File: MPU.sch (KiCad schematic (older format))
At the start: 31 parts, among them P1 BL_PAD, P10 CONN_01X01, P11 CONN_01X04, P2 SWD_DAT, P3 SWD_CLK, P4 SWD_3V3, P5 SWD_GND, P6 SWD_RST, P7 CONN_01X01, P8 CONN_01X01, P9 CONN_01X01, SW1 SW_PUSH, SW2 SW_PUSH, U4 SAMD21E17A, Y1 32.768kHz

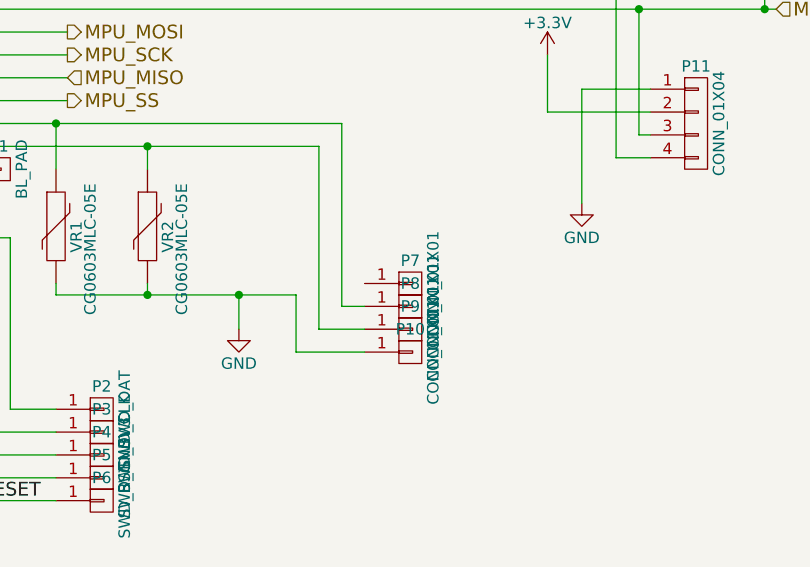
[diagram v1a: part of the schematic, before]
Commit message: moved battery input and fixed dodgy ground plane
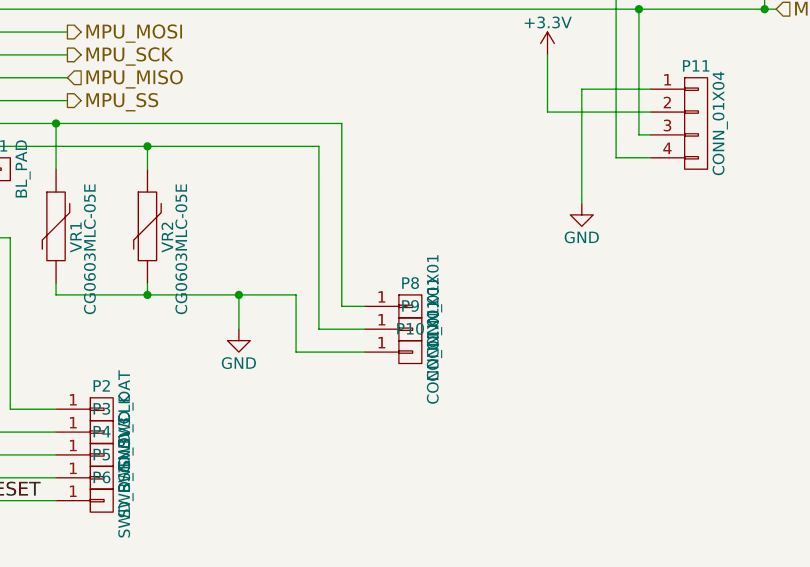
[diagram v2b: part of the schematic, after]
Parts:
- removed P7: CONN_01X01, Measurement_Points:Measurement_Point_Round-TH_Small, symbol CONN_01X01
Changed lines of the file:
@@
 $EndComp
 $Comp
-L GND #PWR013
+L GND #PWR26
 U 1 1 56C13132
 P 6950 4550
-F 0 "#PWR013" H 6950 4300 50  0001 C CNN
+F 0 "#PWR26" H 6950 4300 50  0001 C CNN
 F 1 "GND" H 6950 4400 50  0000 C CNN
 F 2 "" H 6950 4550 50  0000 C CNN
@@
 Connection ~ 2200 2050
 $Comp
-L GND #PWR014
+L GND #PWR15
 U 1 1 56C1336E
 P 1900 2650
-F 0 "#PWR014" H 1900 2400 50  0001 C CNN
+F 0 "#PWR15" H 1900 2400 50  0001 C CNN
 F 1 "GND" H 1900 2500 50  0000 C CNN
 F 2 "" H 1900 2650 50  0000 C CNN
@@
 $EndComp
 $Comp
-L GND #PWR015
+L GND #PWR16
 U 1 1 56C133A0
 P 2200 2650
-F 0 "#PWR015" H 2200 2400 50  0001 C CNN
+F 0 "#PWR16" H 2200 2400 50  0001 C CNN
 F 1 "GND" H 2200 2500 50  0000 C CNN
 F 2 "" H 2200 2650 50  0000 C CNN
@@
 $EndComp
 $Comp
-L GND #PWR016
+L GND #PWR18
 U 1 1 56C133D2
 P 2500 2650
-F 0 "#PWR016" H 2500 2400 50  0001 C CNN
+F 0 "#PWR18" H 2500 2400 50  0001 C CNN
 F 1 "GND" H 2500 2500 50  0000 C CNN
 F 2 "" H 2500 2650 50  0000 C CNN
@@
 $EndComp
 $Comp
-L +3V3 #PWR017
+L +3V3 #PWR30
 U 1 1 56C24D00
 P 9150 2500
-F 0 "#PWR017" H 9150 2350 50  0001 C CNN
+F 0 "#PWR30" H 9150 2350 50  0001 C CNN
 F 1 "+3V3" H 9150 2640 50  0000 C CNN
 F 2 "" H 9150 2500 50  0000 C CNN
@@
 $EndComp
 $Comp
-L GND #PWR018
+L GND #PWR25
 U 1 1 56C269FF
 P 6100 1400
-F 0 "#PWR018" H 6100 1150 50  0001 C CNN
+F 0 "#PWR25" H 6100 1150 50  0001 C CNN
 F 1 "GND" H 6100 1250 50  0000 C CNN
 F 2 "" H 6100 1400 50  0000 C CNN
@@
 AIN_6
 $Comp
-L GND #PWR019
+L GND #PWR21
 U 1 1 56C278AB
 P 4000 6000
-F 0 "#PWR019" H 4000 5750 50  0001 C CNN
+F 0 "#PWR21" H 4000 5750 50  0001 C CNN
 F 1 "GND" H 4000 5850 50  0000 C CNN
 F 2 "" H 4000 6000 50  0000 C CNN
@@
 	1550 3000 1550 3200
 $Comp
-L GND #PWR020
+L GND #PWR14
 U 1 1 56C282F2
 P 1550 3600
-F 0 "#PWR020" H 1550 3350 50  0001 C CNN
+F 0 "#PWR14" H 1550 3350 50  0001 C CNN
 F 1 "GND" H 1550 3450 50  0000 C CNN
 F 2 "" H 1550 3600 50  0000 C CNN
@@
 	1550 3500 1550 3600
 $Comp
-L +3V3 #PWR021
+L +3V3 #PWR13
 U 1 1 56C28419
 P 1550 3000
-F 0 "#PWR021" H 1550 2850 50  0001 C CNN
+F 0 "#PWR13" H 1550 2850 50  0001 C CNN
 F 1 "+3V3" H 1550 3140 50  0000 C CNN
 F 2 "" H 1550 3000 50  0000 C CNN
@@
 	2600 1650 2600 1550
 $Comp
-L +3V3 #PWR022
+L +3V3 #PWR19
 U 1 1 56C28F33
 P 2600 1150
-F 0 "#PWR022" H 2600 1000 50  0001 C CNN
+F 0 "#PWR19" H 2600 1000 50  0001 C CNN
 F 1 "+3V3" H 2600 1290 50  0000 C CNN
 F 2 "" H 2600 1150 50  0000 C CNN
@@
 	2600 1150 2600 1250
 $Comp
-L +3V3 #PWR023
+L +3V3 #PWR23
 U 1 1 56C2B080
 P 5350 5050
-F 0 "#PWR023" H 5350 4900 50  0001 C CNN
+F 0 "#PWR23" H 5350 4900 50  0001 C CNN
 F 1 "+3V3" H 5350 5190 50  0000 C CNN
 F 2 "" H 5350 5050 50  0000 C CNN
@@
 $EndComp
 $Comp
-L GND #PWR024
+L GND #PWR24
 U 1 1 56C2B0D0
 P 5350 5250
-F 0 "#PWR024" H 5350 5000 50  0001 C CNN
+F 0 "#PWR24" H 5350 5000 50  0001 C CNN
 F 1 "GND" H 5350 5100 50  0000 C CNN
 F 2 "" H 5350 5250 50  0000 C CNN
@@
 	5350 5200 6150 5200
 $Comp
-L +3V3 #PWR025
+L +3V3 #PWR17
 U 1 1 56C2B3B6
 P 2350 1900
-F 0 "#PWR025" H 2350 1750 50  0001 C CNN
+F 0 "#PWR17" H 2350 1750 50  0001 C CNN
 F 1 "+3V3" H 2350 2040 50  0000 C CNN
 F 2 "" H 2350 1900 50  0000 C CNN
@@
 Connection ~ 2350 2050
 $Comp
-L GND #PWR026
+L GND #PWR20
 U 1 1 56C39EB2
 P 2900 4300
-F 0 "#PWR026" H 2900 4050 50  0001 C CNN
+F 0 "#PWR20" H 2900 4050 50  0001 C CNN
 F 1 "GND" H 2900 4150 50  0000 C CNN
 F 2 "" H 2900 4300 50  0000 C CNN
@@
 	4700 6200 4700 6050
 $Comp
-L +3V3 #PWR027
+L +3V3 #PWR22
 U 1 1 56C3A13C
 P 4700 5100
-F 0 "#PWR027" H 4700 4950 50  0001 C CNN
+F 0 "#PWR22" H 4700 4950 50  0001 C CNN
 F 1 "+3V3" H 4700 5240 50  0000 C CNN
 F 2 "" H 4700 5100 50  0000 C CNN
@@
 F 3 "" H 6350 5300 50  0000 C CNN
 	1    6350 5300
-	1    0    0    -1
-$EndComp
-$Comp
-L CONN_01X01 P7
-U 1 1 56C3BDC8
-P 7700 4350
-F 0 "P7" H 7700 4450 50  0000 C CNN
-F 1 "CONN_01X01" V 7800 4350 50  0000 C CNN
-F 2 "Measurement_Points:Measurement_Point_Round-TH_Small" H 7700 4350 50  0001 C CNN
-F 3 "" H 7700 4350 50  0000 C CNN
-	1    7700 4350
 	1    0    0    -1
 $EndComp
@@
 $EndComp
 $Comp
-L GND #PWR028
+L GND #PWR28
 U 1 1 56EAE5DD
 P 8450 4000
-F 0 "#PWR028" H 8450 3750 50  0001 C CNN
+F 0 "#PWR28" H 8450 3750 50  0001 C CNN
 F 1 "GND" H 8450 3850 50  0000 C CNN
 F 2 "" H 8450 4000 50  0000 C CNN
@@
 $EndComp
 $Comp
-L +3.3V #PWR029
+L +3.3V #PWR27
 U 1 1 56EAE62B
 P 8300 3350
-F 0 "#PWR029" H 8300 3200 50  0001 C CNN
+F 0 "#PWR27" H 8300 3200 50  0001 C CNN
 F 1 "+3.3V" H 8300 3490 50  0000 C CNN
 F 2 "" H 8300 3350 50  0000 C CNN
@@
 $EndComp
 $Comp
-L GND #PWR030
+L GND #PWR29
 U 1 1 56EC2766
 P 8750 2600
-F 0 "#PWR030" H 8750 2350 50  0001 C CNN
+F 0 "#PWR29" H 8750 2350 50  0001 C CNN
 F 1 "GND" H 8750 2450 50  0000 C CNN
 F 2 "" H 8750 2600 50  0000 C CNN

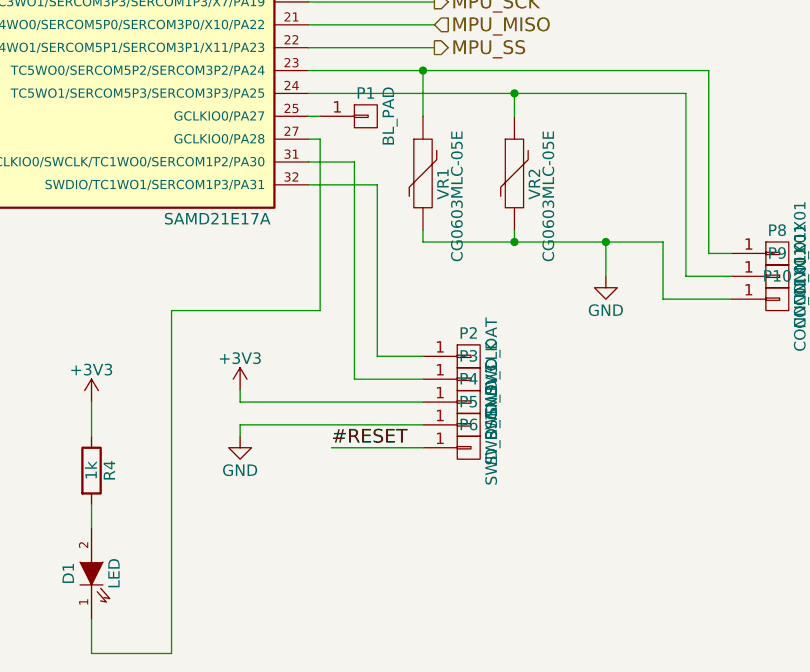
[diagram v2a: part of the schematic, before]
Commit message: Changed L3 to 0603, L2 to 3x3, Fixed P8 silk and made gerbers
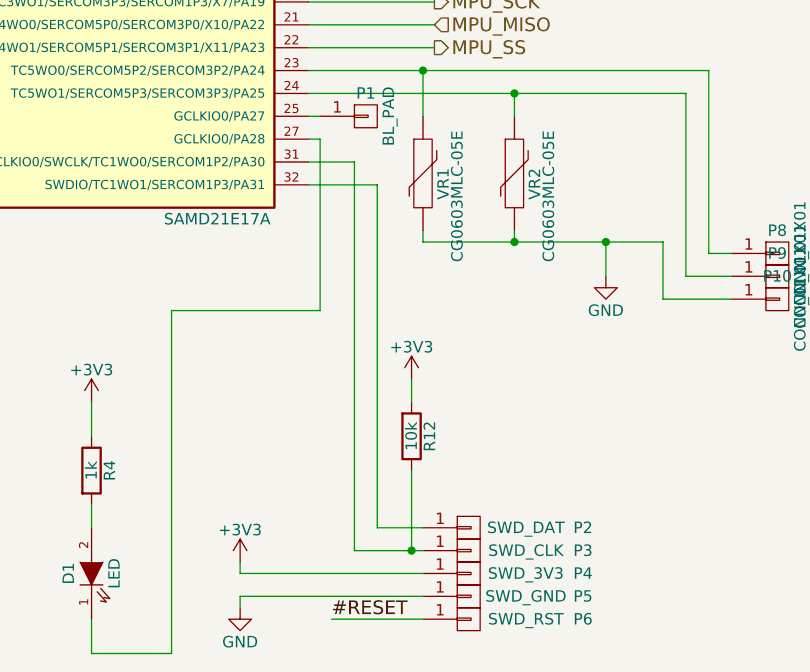
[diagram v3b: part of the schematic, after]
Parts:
- added R12: 10k, Capacitors_SMD:C_0603, symbol R
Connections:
- net +3V3: now also R12.2
- net at P3.1 (P1), U4.31 (GCLKIO0/SWCLK/TC1WO0/SERCOM1P2/PA30): now also R12.1
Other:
- moved on the sheet: P2, P3, P4, P5, P6
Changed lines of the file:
@@
 $EndComp
 $Comp
-L GND #PWR26
+L GND #PWR013
 U 1 1 56C13132
 P 6950 4550
-F 0 "#PWR26" H 6950 4300 50  0001 C CNN
+F 0 "#PWR013" H 6950 4300 50  0001 C CNN
 F 1 "GND" H 6950 4400 50  0000 C CNN
 F 2 "" H 6950 4550 50  0000 C CNN
@@
 Connection ~ 2200 2050
 $Comp
-L GND #PWR15
+L GND #PWR014
 U 1 1 56C1336E
 P 1900 2650
-F 0 "#PWR15" H 1900 2400 50  0001 C CNN
+F 0 "#PWR014" H 1900 2400 50  0001 C CNN
 F 1 "GND" H 1900 2500 50  0000 C CNN
 F 2 "" H 1900 2650 50  0000 C CNN
@@
 $EndComp
 $Comp
-L GND #PWR16
+L GND #PWR015
 U 1 1 56C133A0
 P 2200 2650
-F 0 "#PWR16" H 2200 2400 50  0001 C CNN
+F 0 "#PWR015" H 2200 2400 50  0001 C CNN
 F 1 "GND" H 2200 2500 50  0000 C CNN
 F 2 "" H 2200 2650 50  0000 C CNN
@@
 $EndComp
 $Comp
-L GND #PWR18
+L GND #PWR016
 U 1 1 56C133D2
 P 2500 2650
-F 0 "#PWR18" H 2500 2400 50  0001 C CNN
+F 0 "#PWR016" H 2500 2400 50  0001 C CNN
 F 1 "GND" H 2500 2500 50  0000 C CNN
 F 2 "" H 2500 2650 50  0000 C CNN
@@
 $EndComp
 $Comp
-L +3V3 #PWR30
+L +3V3 #PWR017
 U 1 1 56C24D00
 P 9150 2500
-F 0 "#PWR30" H 9150 2350 50  0001 C CNN
+F 0 "#PWR017" H 9150 2350 50  0001 C CNN
 F 1 "+3V3" H 9150 2640 50  0000 C CNN
 F 2 "" H 9150 2500 50  0000 C CNN
@@
 $EndComp
 $Comp
-L GND #PWR25
+L GND #PWR018
 U 1 1 56C269FF
 P 6100 1400
-F 0 "#PWR25" H 6100 1150 50  0001 C CNN
+F 0 "#PWR018" H 6100 1150 50  0001 C CNN
 F 1 "GND" H 6100 1250 50  0000 C CNN
 F 2 "" H 6100 1400 50  0000 C CNN
@@
 AIN_6
 $Comp
-L GND #PWR21
+L GND #PWR019
 U 1 1 56C278AB
 P 4000 6000
-F 0 "#PWR21" H 4000 5750 50  0001 C CNN
+F 0 "#PWR019" H 4000 5750 50  0001 C CNN
 F 1 "GND" H 4000 5850 50  0000 C CNN
 F 2 "" H 4000 6000 50  0000 C CNN
@@
 	1550 3000 1550 3200
 $Comp
-L GND #PWR14
+L GND #PWR020
 U 1 1 56C282F2
 P 1550 3600
-F 0 "#PWR14" H 1550 3350 50  0001 C CNN
+F 0 "#PWR020" H 1550 3350 50  0001 C CNN
 F 1 "GND" H 1550 3450 50  0000 C CNN
 F 2 "" H 1550 3600 50  0000 C CNN
@@
 	1550 3500 1550 3600
 $Comp
-L +3V3 #PWR13
+L +3V3 #PWR021
 U 1 1 56C28419
 P 1550 3000
-F 0 "#PWR13" H 1550 2850 50  0001 C CNN
+F 0 "#PWR021" H 1550 2850 50  0001 C CNN
 F 1 "+3V3" H 1550 3140 50  0000 C CNN
 F 2 "" H 1550 3000 50  0000 C CNN
@@
 	5650 4050 5850 4050
 Wire Wire Line
-	5850 4050 5850 5000
-Wire Wire Line
-	5850 5000 6150 5000
-Wire Wire Line
-	6150 4900 5950 4900
-Wire Wire Line
-	5950 4900 5950 4150
+	5850 4050 5850 5750
+Wire Wire Line
+	5850 5750 6150 5750
+Wire Wire Line
+	5950 5650 6150 5650
+Wire Wire Line
+	5950 4150 5950 5650
 Wire Wire Line
 	5950 4150 5650 4150
@@
 #RESET
 Wire Wire Line
-	6150 5300 5750 5300
-Text Label 5750 5300 0    60   ~ 0
+	6150 6050 5750 6050
+Text Label 5750 6050 0    60   ~ 0
 #RESET
 $Comp
@@
 	2600 1650 2600 1550
 $Comp
-L +3V3 #PWR19
+L +3V3 #PWR022
 U 1 1 56C28F33
 P 2600 1150
-F 0 "#PWR19" H 2600 1000 50  0001 C CNN
+F 0 "#PWR022" H 2600 1000 50  0001 C CNN
 F 1 "+3V3" H 2600 1290 50  0000 C CNN
 F 2 "" H 2600 1150 50  0000 C CNN
@@
 	2600 1150 2600 1250
 $Comp
-L +3V3 #PWR23
+L +3V3 #PWR023
 U 1 1 56C2B080
-P 5350 5050
-F 0 "#PWR23" H 5350 4900 50  0001 C CNN
-F 1 "+3V3" H 5350 5190 50  0000 C CNN
-F 2 "" H 5350 5050 50  0000 C CNN
-F 3 "" H 5350 5050 50  0000 C CNN
-	1    5350 5050
-	1    0    0    -1
-$EndComp
-$Comp
-L GND #PWR24
+P 5350 5800
+F 0 "#PWR023" H 5350 5650 50  0001 C CNN
+F 1 "+3V3" H 5350 5940 50  0000 C CNN
+F 2 "" H 5350 5800 50  0000 C CNN
+F 3 "" H 5350 5800 50  0000 C CNN
+	1    5350 5800
+	1    0    0    -1
+$EndComp
+$Comp
+L GND #PWR024
 U 1 1 56C2B0D0
-P 5350 5250
-F 0 "#PWR24" H 5350 5000 50  0001 C CNN
-F 1 "GND" H 5350 5100 50  0000 C CNN
-F 2 "" H 5350 5250 50  0000 C CNN
-F 3 "" H 5350 5250 50  0000 C CNN
-	1    5350 5250
-	1    0    0    -1
-$EndComp
-Wire Wire Line
-	5350 5050 5350 5100
-Wire Wire Line
-	5350 5100 6150 5100
-Wire Wire Line
-	5350 5250 5350 5200
-Wire Wire Line
-	5350 5200 6150 5200
-$Comp
-L +3V3 #PWR17
+P 5350 6000
+F 0 "#PWR024" H 5350 5750 50  0001 C CNN
+F 1 "GND" H 5350 5850 50  0000 C CNN
+F 2 "" H 5350 6000 50  0000 C CNN
+F 3 "" H 5350 6000 50  0000 C CNN
+	1    5350 6000
+	1    0    0    -1
+$EndComp
+Wire Wire Line
+	5350 5800 5350 5850
+Wire Wire Line
+	5350 5850 6150 5850
+Wire Wire Line
+	5350 6000 5350 5950
+Wire Wire Line
+	5350 5950 6150 5950
+$Comp
+L +3V3 #PWR025
 U 1 1 56C2B3B6
 P 2350 1900
-F 0 "#PWR17" H 2350 1750 50  0001 C CNN
+F 0 "#PWR025" H 2350 1750 50  0001 C CNN
 F 1 "+3V3" H 2350 2040 50  0000 C CNN
 F 2 "" H 2350 1900 50  0000 C CNN
@@
 Connection ~ 2350 2050
 $Comp
-L GND #PWR20
+L GND #PWR026
 U 1 1 56C39EB2
 P 2900 4300
-F 0 "#PWR20" H 2900 4050 50  0001 C CNN
+F 0 "#PWR026" H 2900 4050 50  0001 C CNN
 F 1 "GND" H 2900 4150 50  0000 C CNN
 F 2 "" H 2900 4300 50  0000 C CNN
@@
 	4700 6200 4700 6050
 $Comp
-L +3V3 #PWR22
+L +3V3 #PWR027
 U 1 1 56C3A13C
 P 4700 5100
-F 0 "#PWR22" H 4700 4950 50  0001 C CNN
+F 0 "#PWR027" H 4700 4950 50  0001 C CNN
 F 1 "+3V3" H 4700 5240 50  0000 C CNN
 F 2 "" H 4700 5100 50  0000 C CNN
@@
 L CONN_01X01 P2
 U 1 1 56C3B65F
-P 6350 4900
-F 0 "P2" H 6350 5000 50  0000 C CNN
-F 1 "SWD_DAT" V 6450 4900 50  0000 C CNN
-F 2 "Measurement_Points:Measurement_Point_Round-TH_Small" H 6350 4900 50  0001 C CNN
-F 3 "" H 6350 4900 50  0000 C CNN
-	1    6350 4900
+P 6350 5650
+F 0 "P2" H 6850 5650 50  0000 C CNN
+F 1 "SWD_DAT" H 6600 5650 50  0000 C CNN
+F 2 "Measurement_Points:Measurement_Point_Round-TH_Small" H 6350 5650 50  0001 C CNN
+F 3 "" H 6350 5650 50  0000 C CNN
+	1    6350 5650
 	1    0    0    -1
 $EndComp
@@
 L CONN_01X01 P3
 U 1 1 56C3B6CD
-P 6350 5000
-F 0 "P3" H 6350 5100 50  0000 C CNN
-F 1 "SWD_CLK" V 6450 5000 50  0000 C CNN
-F 2 "Measurement_Points:Measurement_Point_Round-TH_Small" H 6350 5000 50  0001 C CNN
-F 3 "" H 6350 5000 50  0000 C CNN
-	1    6350 5000
+P 6350 5750
+F 0 "P3" H 6850 5750 50  0000 C CNN
+F 1 "SWD_CLK" H 6600 5750 50  0000 C CNN
+F 2 "Measurement_Points:Measurement_Point_Round-TH_Small" H 6350 5750 50  0001 C CNN
+F 3 "" H 6350 5750 50  0000 C CNN
+	1    6350 5750
 	1    0    0    -1
 $EndComp
@@
 L CONN_01X01 P4
 U 1 1 56C3B72A
-P 6350 5100
-F 0 "P4" H 6350 5200 50  0000 C CNN
-F 1 "SWD_3V3" V 6450 5100 50  0000 C CNN
-F 2 "Measurement_Points:Measurement_Point_Round-TH_Small" H 6350 5100 50  0001 C CNN
-F 3 "" H 6350 5100 50  0000 C CNN
-	1    6350 5100
+P 6350 5850
+F 0 "P4" H 6850 5850 50  0000 C CNN
+F 1 "SWD_3V3" H 6600 5850 50  0000 C CNN
+F 2 "Measurement_Points:Measurement_Point_Round-TH_Small" H 6350 5850 50  0001 C CNN
+F 3 "" H 6350 5850 50  0000 C CNN
+	1    6350 5850
 	1    0    0    -1
 $EndComp
@@
 L CONN_01X01 P5
 U 1 1 56C3B78A
-P 6350 5200
-F 0 "P5" H 6350 5300 50  0000 C CNN
-F 1 "SWD_GND" V 6450 5200 50  0000 C CNN
-F 2 "Measurement_Points:Measurement_Point_Round-TH_Small" H 6350 5200 50  0001 C CNN
-F 3 "" H 6350 5200 50  0000 C CNN
-	1    6350 5200
+P 6350 5950
+F 0 "P5" H 6850 5950 50  0000 C CNN
+F 1 "SWD_GND" H 6600 5950 50  0000 C CNN
+F 2 "Measurement_Points:Measurement_Point_Round-TH_Small" H 6350 5950 50  0001 C CNN
+F 3 "" H 6350 5950 50  0000 C CNN
+	1    6350 5950
 	1    0    0    -1
 $EndComp
@@
 L CONN_01X01 P6
 U 1 1 56C3BA50
-P 6350 5300
-F 0 "P6" H 6350 5400 50  0000 C CNN
-F 1 "SWD_RST" V 6450 5300 50  0000 C CNN
-F 2 "Measurement_Points:Measurement_Point_Round-TH_Small" H 6350 5300 50  0001 C CNN
-F 3 "" H 6350 5300 50  0000 C CNN
-	1    6350 5300
+P 6350 6050
+F 0 "P6" H 6850 6050 50  0000 C CNN
+F 1 "SWD_RST" H 6600 6050 50  0000 C CNN
+F 2 "Measurement_Points:Measurement_Point_Round-TH_Small" H 6350 6050 50  0001 C CNN
+F 3 "" H 6350 6050 50  0000 C CNN
+	1    6350 6050
 	1    0    0    -1
 $EndComp
@@
 $EndComp
 $Comp
-L GND #PWR28
+L GND #PWR028
 U 1 1 56EAE5DD
 P 8450 4000
-F 0 "#PWR28" H 8450 3750 50  0001 C CNN
+F 0 "#PWR028" H 8450 3750 50  0001 C CNN
 F 1 "GND" H 8450 3850 50  0000 C CNN
 F 2 "" H 8450 4000 50  0000 C CNN
@@
 $EndComp
 $Comp
-L +3.3V #PWR27
+L +3.3V #PWR029
 U 1 1 56EAE62B
 P 8300 3350
-F 0 "#PWR27" H 8300 3200 50  0001 C CNN
+F 0 "#PWR029" H 8300 3200 50  0001 C CNN
 F 1 "+3.3V" H 8300 3490 50  0000 C CNN
 F 2 "" H 8300 3350 50  0000 C CNN
@@
 $EndComp
 $Comp
-L GND #PWR29
+L GND #PWR030
 U 1 1 56EC2766
 P 8750 2600
-F 0 "#PWR29" H 8750 2350 50  0001 C CNN
+F 0 "#PWR030" H 8750 2350 50  0001 C CNN
 F 1 "GND" H 8750 2450 50  0000 C CNN
 F 2 "" H 8750 2600 50  0000 C CNN
@@
 Wire Wire Line
 	7850 2350 8050 2350
+$Comp
+L R R12
+U 1 1 56F9003D
+P 6100 5250
+F 0 "R12" V 6180 5250 50  0000 C CNN
+F 1 "10k" V 6100 5250 50  0000 C CNN
+F 2 "Capacitors_SMD:C_0603" V 6030 5250 50  0001 C CNN
+F 3 "" H 6100 5250 50  0000 C CNN
+	1    6100 5250
+	1    0    0    1
+$EndComp
+$Comp
+L +3V3 #PWR031
+U 1 1 56F90C8F
+P 6100 5000
+F 0 "#PWR031" H 6100 4850 50  0001 C CNN
+F 1 "+3V3" H 6100 5140 50  0000 C CNN
+F 2 "" H 6100 5000 50  0000 C CNN
+F 3 "" H 6100 5000 50  0000 C CNN
+	1    6100 5000
+	1    0    0    -1
+$EndComp
+Wire Wire Line
+	6100 5000 6100 5100
+Wire Wire Line
+	6100 5400 6100 5750
+Connection ~ 6100 5750
 $EndSCHEMATC

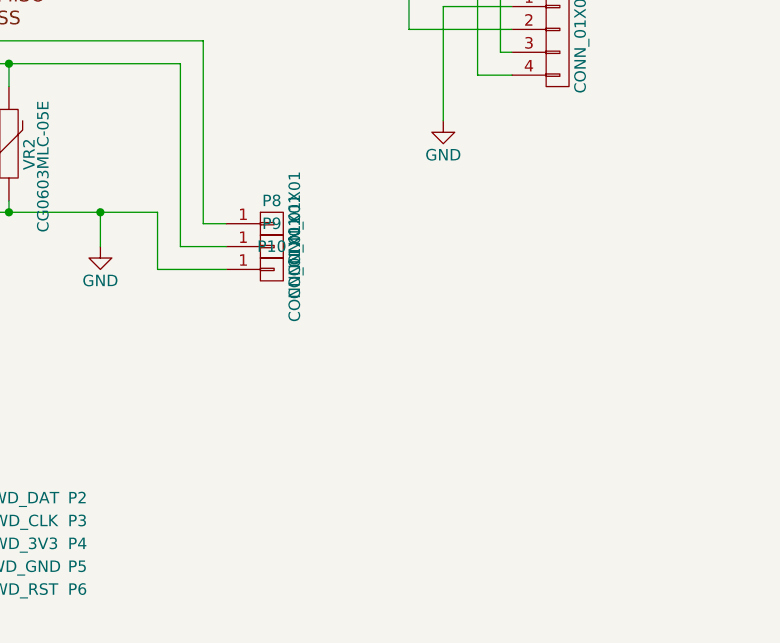
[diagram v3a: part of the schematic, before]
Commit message: Started changes after first round, micro usb connector, fixing footprint for accelerometer
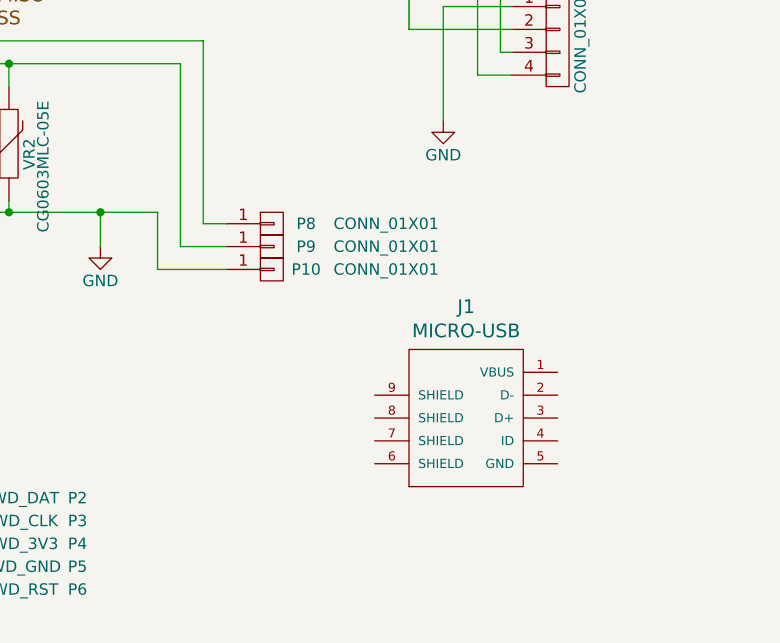
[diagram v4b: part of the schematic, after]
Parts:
- added J1: MICRO-USB, RocketScreamKicadLibrary:MICRO-USB, symbol MICRO-USB
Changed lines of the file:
@@
 U 1 1 56C3BE2F
 P 7700 4450
-F 0 "P8" H 7700 4550 50  0000 C CNN
-F 1 "CONN_01X01" V 7800 4450 50  0000 C CNN
+F 0 "P8" H 7850 4450 50  0000 C CNN
+F 1 "CONN_01X01" H 8200 4450 50  0000 C CNN
 F 2 "Measurement_Points:Measurement_Point_Round-TH_Small" H 7700 4450 50  0001 C CNN
 F 3 "" H 7700 4450 50  0000 C CNN
@@
 U 1 1 56C3BE98
 P 7700 4550
-F 0 "P9" H 7700 4650 50  0000 C CNN
-F 1 "CONN_01X01" V 7800 4550 50  0000 C CNN
+F 0 "P9" H 7850 4550 50  0000 C CNN
+F 1 "CONN_01X01" H 8200 4550 50  0000 C CNN
 F 2 "Measurement_Points:Measurement_Point_Round-TH_Small" H 7700 4550 50  0001 C CNN
 F 3 "" H 7700 4550 50  0000 C CNN
@@
 U 1 1 56C3BF04
 P 7700 4650
-F 0 "P10" H 7700 4750 50  0000 C CNN
-F 1 "CONN_01X01" V 7800 4650 50  0000 C CNN
+F 0 "P10" H 7850 4650 50  0000 C CNN
+F 1 "CONN_01X01" H 8200 4650 50  0000 C CNN
 F 2 "Measurement_Points:Measurement_Point_Round-TH_Small" H 7700 4650 50  0001 C CNN
 F 3 "" H 7700 4650 50  0000 C CNN
@@
 	6100 5400 6100 5750
 Connection ~ 6100 5750
+$Comp
+L MICRO-USB J1
+U 1 1 5700ADCA
+P 8550 5300
+F 0 "J1" H 8550 5787 60  0000 C CNN
+F 1 "MICRO-USB" H 8550 5681 60  0000 C CNN
+F 2 "RocketScreamKicadLibrary:MICRO-USB" H 8550 4850 60  0001 C CNN
+F 3 "" H 8600 5500 60  0000 C CNN
+	1    8550 5300
+	1    0    0    -1
+$EndComp
 $EndSCHEMATC
